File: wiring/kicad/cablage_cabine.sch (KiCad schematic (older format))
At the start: 20 parts, among them J1 Jack90, J2 USB-µ, J3 AlimPlug, SW1 Poussoir, U1 RJ45_Through, U10 Nappe, U11 sortie230, U12 sortie230, U13 FLASH, U14 1200D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

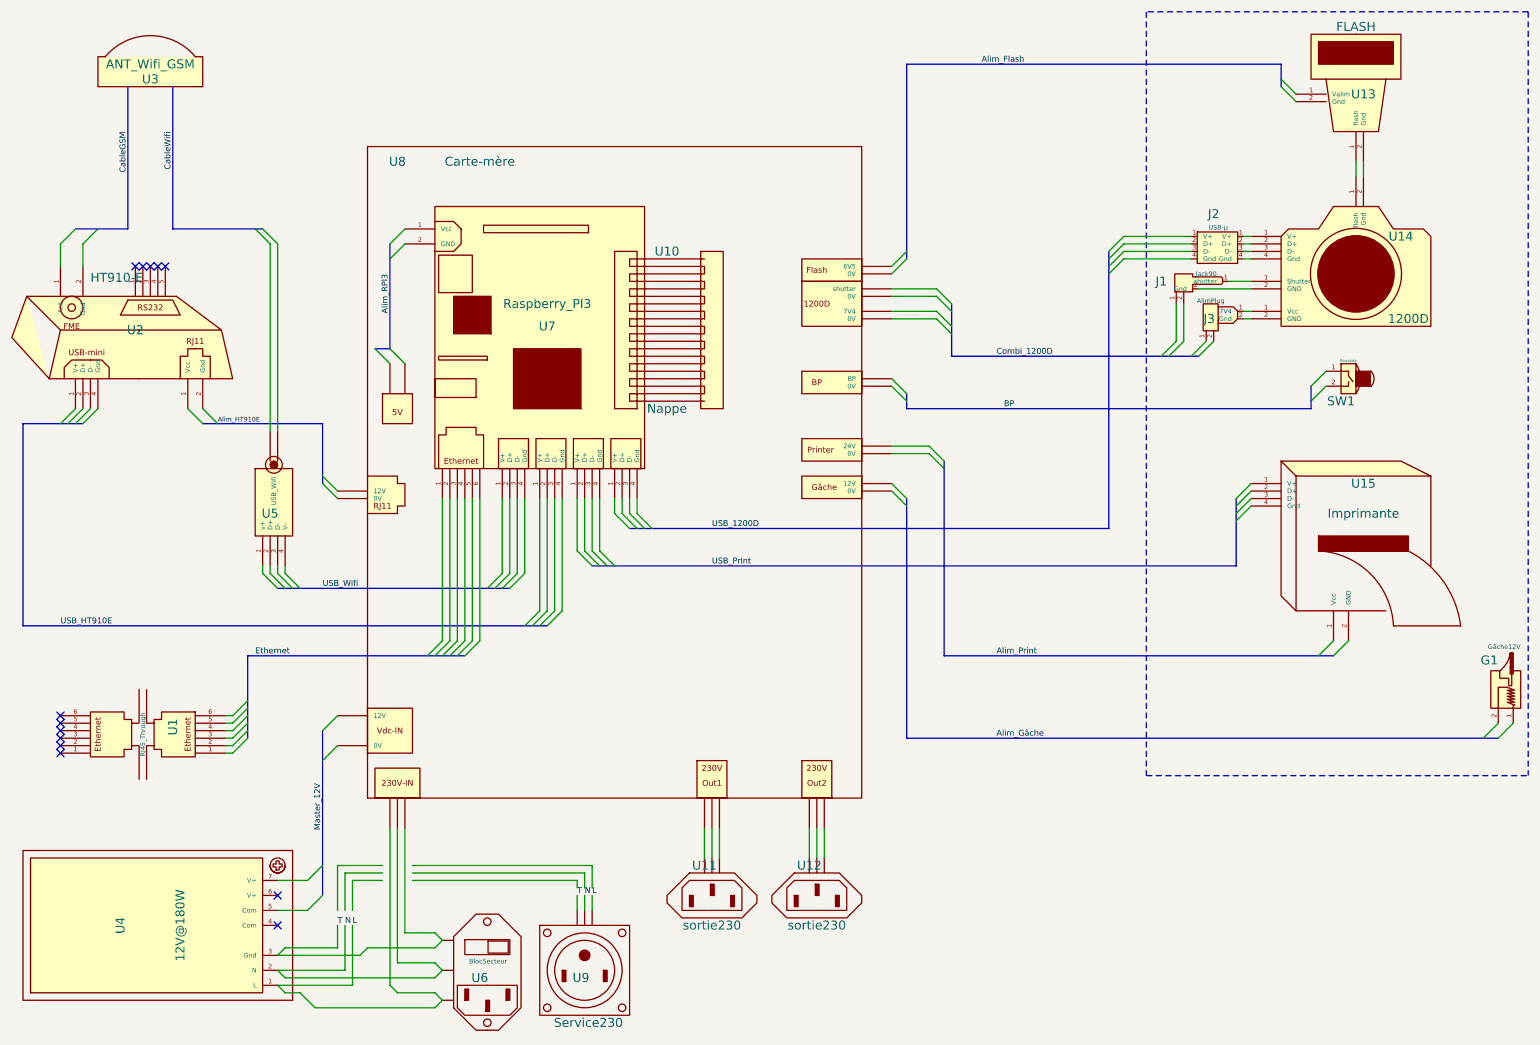
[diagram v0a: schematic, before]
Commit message: * Modification du plan de câblage. Définition des bretelles pour la partie secteur.
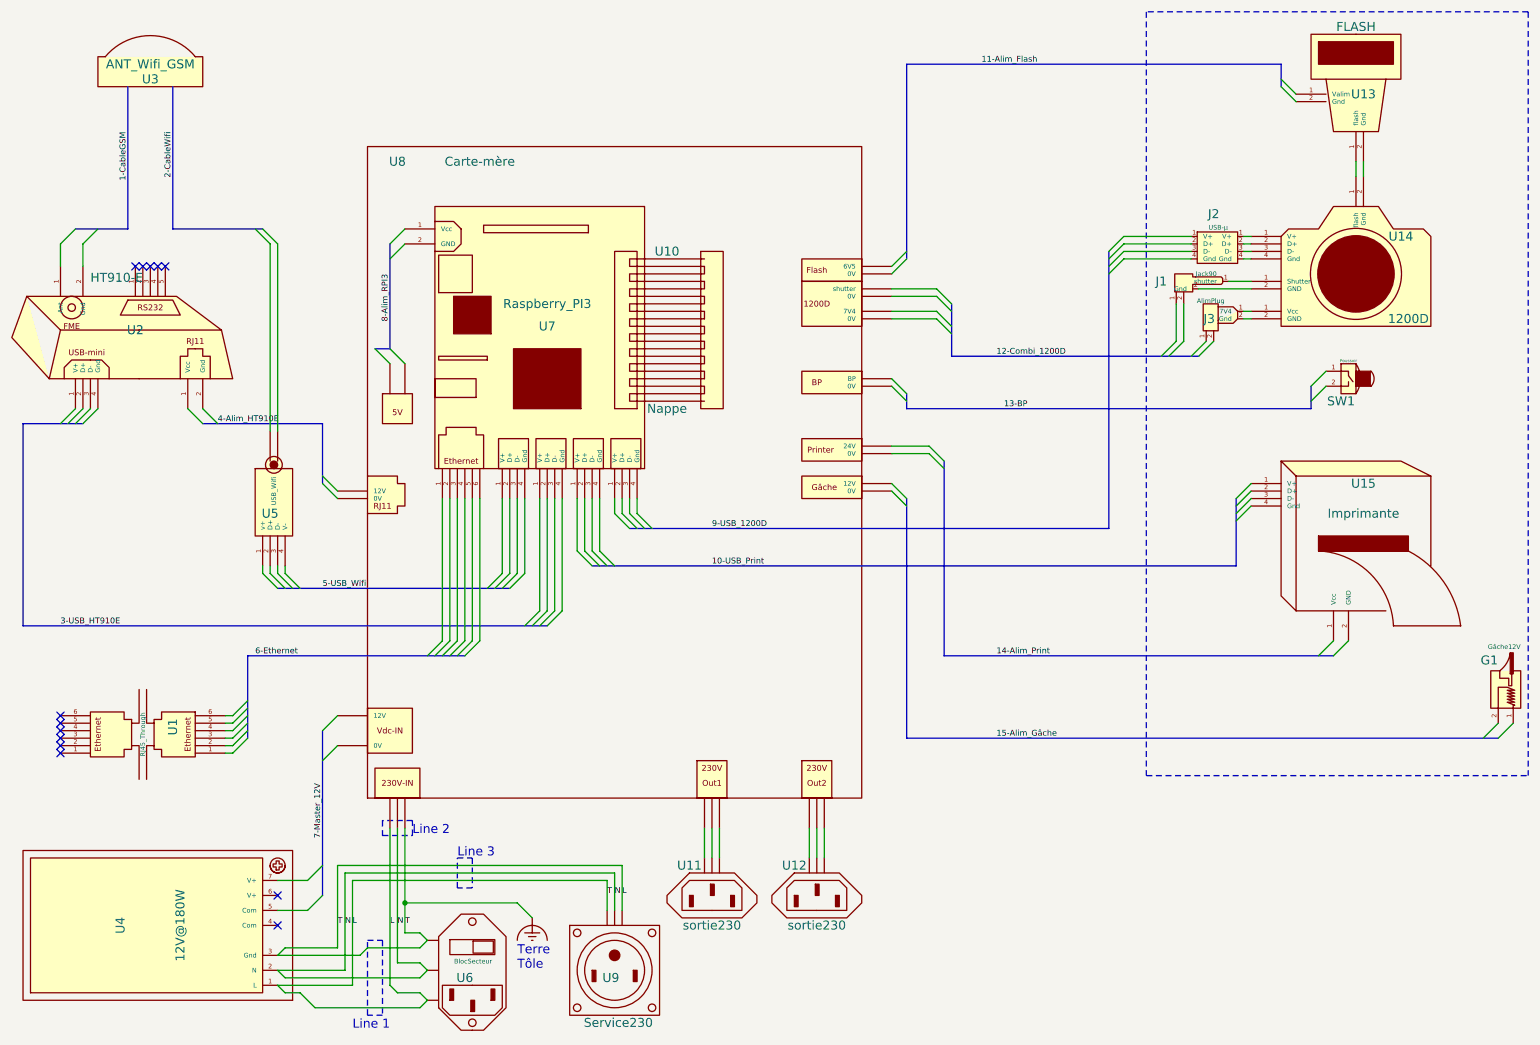
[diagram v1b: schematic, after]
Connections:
- net labels added: 1-CableGSM, 10-USB_Print, 11-Alim_Flash, 12-Combi_1200D, 13-BP, 14-Alim_Print, 15-Alim_Gâche, 2-CableWifi, 3-USB_HT910E, 4-Alim_HT910E, 5-USB_Wifi, 6-Ethernet, 7-Master_12V, 8-Alim_RPI3, 9-USB_1200D, Earth_Clean
- net labels removed: Alim_Flash, Alim_Gâche, Alim_HT910E, Alim_Print, Alim_RPI3, BP, CableGSM, CableWifi, Combi_1200D, Ethernet, Master_12V, USB_1200D, USB_HT910E, USB_Print, USB_Wifi
- wire segments 110 -> 103
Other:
- note added: "Line 1"
- note added: "Line 2"
- note added: "Line 3"
- note added: "Terre\nTôle"
- moved on the sheet: U6, U9
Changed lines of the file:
@@
 U 1 1 58E76E27
 P 5300 6650
-F 0 "U11" H 5250 6800 60  0000 C CNN
+F 0 "U11" H 5150 6800 60  0000 C CNN
 F 1 "sortie230" H 5300 6400 60  0000 C CNN
 F 2 "" H 5315 6650 60  0001 C CNN
@@
 U 1 1 58E76F6F
 P 6000 6650
-F 0 "U12" H 5950 6800 60  0000 C CNN
+F 0 "U12" H 5850 6800 60  0000 C CNN
 F 1 "sortie230" H 6000 6400 60  0000 C CNN
 F 2 "" H 6015 6650 60  0001 C CNN
@@
 L BlocSecteur U6
 U 1 1 58E771CC
-P 3800 7350
-F 0 "U6" H 3750 7450 60  0000 C CNN
-F 1 "BlocSecteur" H 3805 7560 31  0000 C CNN
-F 2 "" H 3815 7250 60  0001 C CNN
-F 3 "" H 3815 7250 60  0001 C CNN
-	1    3800 7350
+P 3700 7350
+F 0 "U6" H 3650 7450 60  0000 C CNN
+F 1 "BlocSecteur" H 3705 7560 31  0000 C CNN
+F 2 "" H 3715 7250 60  0001 C CNN
+F 3 "" H 3715 7250 60  0001 C CNN
+	1    3700 7350
 	1    0    0    -1
 $EndComp
@@
 L Service230 U9
 U 1 1 58E79C50
-P 4450 7150
-F 0 "U9" H 4425 7050 60  0000 C CNN
-F 1 "Service230" H 4475 6750 60  0000 C CNN
-F 2 "" H 5365 7300 60  0001 C CNN
-F 3 "" H 5365 7300 60  0001 C CNN
-	1    4450 7150
+P 4650 7150
+F 0 "U9" H 4625 7050 60  0000 C CNN
+F 1 "Service230" H 4675 6750 60  0000 C CNN
+F 2 "" H 5565 7300 60  0001 C CNN
+F 3 "" H 5565 7300 60  0001 C CNN
+	1    4650 7150
 	1    0    0    -1
 $EndComp
@@
 $EndComp
 Text Label 1700 1600 3    39   ~ 0
-CableWifi
+2-CableWifi
 Text Label 1400 1600 3    39   ~ 0
-CableGSM
+1-CableGSM
 Text Label 950  4900 0    39   ~ 0
-USB_HT910E
-Text Label 2000 3550 0    31   ~ 0
-Alim_HT910E
+3-USB_HT910E
+Text Label 2000 3550 0    39   ~ 0
+4-Alim_HT910E
 Text Label 2250 5100 0    39   ~ 0
-Ethernet
+6-Ethernet
 Text Label 2700 5950 3    39   ~ 0
-Master_12V
+7-Master_12V
 Text Label 2700 4650 0    39   ~ 0
-USB_Wifi
+5-USB_Wifi
 Text Label 3150 2550 3    39   ~ 0
-Alim_RPI3
+8-Alim_RPI3
 Text Label 7100 1150 0    39   ~ 0
-Alim_Flash
+11-Alim_Flash
 Text Label 7200 3100 0    39   ~ 0
-Combi_1200D
+12-Combi_1200D
 Text Label 7250 3450 0    39   ~ 0
-BP
+13-BP
 Text Label 5300 4250 0    39   ~ 0
-USB_1200D
+9-USB_1200D
 Text Label 5300 4500 0    39   ~ 0
-USB_Print
+10-USB_Print
 Text Label 7200 5100 0    39   ~ 0
-Alim_Print
+14-Alim_Print
 Text Label 7200 5650 0    39   ~ 0
-Alim_Gâche
-Wire Wire Line
-	2650 7450 3450 7450
-Wire Wire Line
-	3450 7450 3500 7400
-Wire Wire Line
-	3500 7400 3450 7350
-Wire Wire Line
-	3450 7350 3200 7350
+15-Alim_Gâche
+Wire Wire Line
+	2650 7450 3350 7450
+Wire Wire Line
+	3350 7450 3400 7400
+Wire Wire Line
+	3400 7400 3350 7350
+Wire Wire Line
+	3350 7350 3200 7350
 Wire Wire Line
 	3200 7350 3150 7300
@@
 	3150 7300 3150 6250
 Wire Wire Line
-	3450 7250 3500 7200
-Wire Wire Line
-	3500 7200 3450 7150
-Wire Wire Line
-	3450 7150 3200 7150
+	3350 7250 3400 7200
+Wire Wire Line
+	3400 7200 3350 7150
+Wire Wire Line
+	3350 7150 3200 7150
 Wire Wire Line
 	3200 7150 3200 6250
 Wire Wire Line
-	3450 7050 3500 7000
-Wire Wire Line
-	3500 7000 3450 6950
-Wire Wire Line
-	3450 6950 3250 6950
+	3350 7050 3400 7000
+Wire Wire Line
+	3400 7000 3350 6950
+Wire Wire Line
+	3350 6950 3250 6950
 Wire Wire Line
 	3250 6950 3250 6250
 Wire Wire Line
-	2450 7250 3450 7250
+	2450 7250 3350 7250
 Wire Wire Line
 	2400 7100 2450 7050
@@
 	2450 7350 2550 7350
 Wire Wire Line
-	2400 7300 2900 7300
+	2900 7300 2400 7300
 Wire Wire Line
 	2550 7350 2650 7450
@@
 	2950 7100 3000 7050
 Wire Wire Line
-	3000 7050 3450 7050
+	3000 7050 3350 7050
 Wire Wire Line
 	2450 7050 2800 7050
@@
 	2400 7200 2850 7200
 Wire Wire Line
-	4400 6800 4400 6700
-Wire Wire Line
-	4450 6800 4450 6700
-Wire Wire Line
-	4500 6800 4500 6700
-Text Label 4400 6700 0    39   ~ 0
+	4600 6600 4600 6800
+Wire Wire Line
+	4650 6550 4650 6800
+Wire Wire Line
+	4700 6500 4700 6800
+Text Label 4600 6700 0    39   ~ 0
 T
-Text Label 4450 6700 0    39   ~ 0
+Text Label 4650 6700 0    39   ~ 0
 N
-Text Label 4500 6700 0    39   ~ 0
+Text Label 4700 6700 0    39   ~ 0
 L
 Wire Wire Line
@@
 	5350 6250 5350 6450
 Wire Wire Line
-	4400 6650 4400 6600
-Wire Wire Line
-	4400 6600 3300 6600
-Wire Wire Line
-	4450 6650 4450 6550
-Wire Wire Line
-	4450 6550 3300 6550
-Wire Wire Line
-	4500 6650 4500 6500
-Wire Wire Line
-	4500 6500 3300 6500
-Wire Wire Line
-	3100 6500 2800 6500
-Wire Wire Line
-	2800 6500 2800 6800
-Wire Wire Line
-	2850 6800 2850 6550
-Wire Wire Line
-	2850 6550 3100 6550
-Wire Wire Line
-	2900 6800 2900 6600
-Wire Wire Line
-	2900 6600 3100 6600
-Wire Wire Line
-	2800 7050 2800 6900
-Wire Wire Line
-	2850 7200 2850 6900
-Wire Wire Line
-	2900 7300 2900 6900
+	2900 6600 4600 6600
+Wire Wire Line
+	2850 6550 4650 6550
+Wire Wire Line
+	2800 6500 4700 6500
+Wire Wire Line
+	2800 7050 2800 6500
+Wire Wire Line
+	2850 7200 2850 6550
+Wire Wire Line
+	2900 6600 2900 7300
 NoConn ~ 950  5500
 NoConn ~ 950  5550
@@
 NoConn ~ 950  5700
 NoConn ~ 950  5750
+$Comp
+L Earth_Clean #PWR?
+U 1 1 58ECDAF9
+P 4100 6850
+F 0 "#PWR?" H 4350 6850 50  0001 C CNN
+F 1 "Earth_Clean" H 4400 6700 50  0001 C CNN
+F 2 "" H 4100 6800 50  0001 C CNN
+F 3 "" H 4100 6800 50  0001 C CNN
+	1    4100 6850
+	1    0    0    -1
+$EndComp
+Text Label 3150 6900 0    39   ~ 0
+L
+Text Label 3200 6900 0    39   ~ 0
+N
+Text Label 3250 6900 0    39   ~ 0
+T
+Wire Notes Line
+	3600 6450 3700 6450
+Wire Notes Line
+	3700 6450 3700 6650
+Wire Notes Line
+	3700 6650 3600 6650
+Wire Notes Line
+	3600 6650 3600 6450
+Wire Notes Line
+	3000 7000 3100 7000
+Wire Notes Line
+	3100 7000 3100 7500
+Wire Notes Line
+	3100 7500 3000 7500
+Wire Notes Line
+	3000 7500 3000 7000
+Wire Notes Line
+	3300 6200 3100 6200
+Wire Notes Line
+	3100 6200 3100 6300
+Wire Notes Line
+	3100 6300 3300 6300
+Wire Notes Line
+	3300 6300 3300 6200
+Text Notes 2900 7600 0    60   ~ 0
+Line 1
+Text Notes 3300 6300 0    60   ~ 0
+Line 2
+Text Notes 3600 6450 0    60   ~ 0
+Line 3
+Wire Wire Line
+	4100 6850 4000 6750
+Wire Wire Line
+	4000 6750 3250 6750
+Connection ~ 3250 6750
+Text Notes 4000 7200 0    60   ~ 0
+Terre\nTôle
 $EndSCHEMATC

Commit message: carte mère V2 et câblage V3
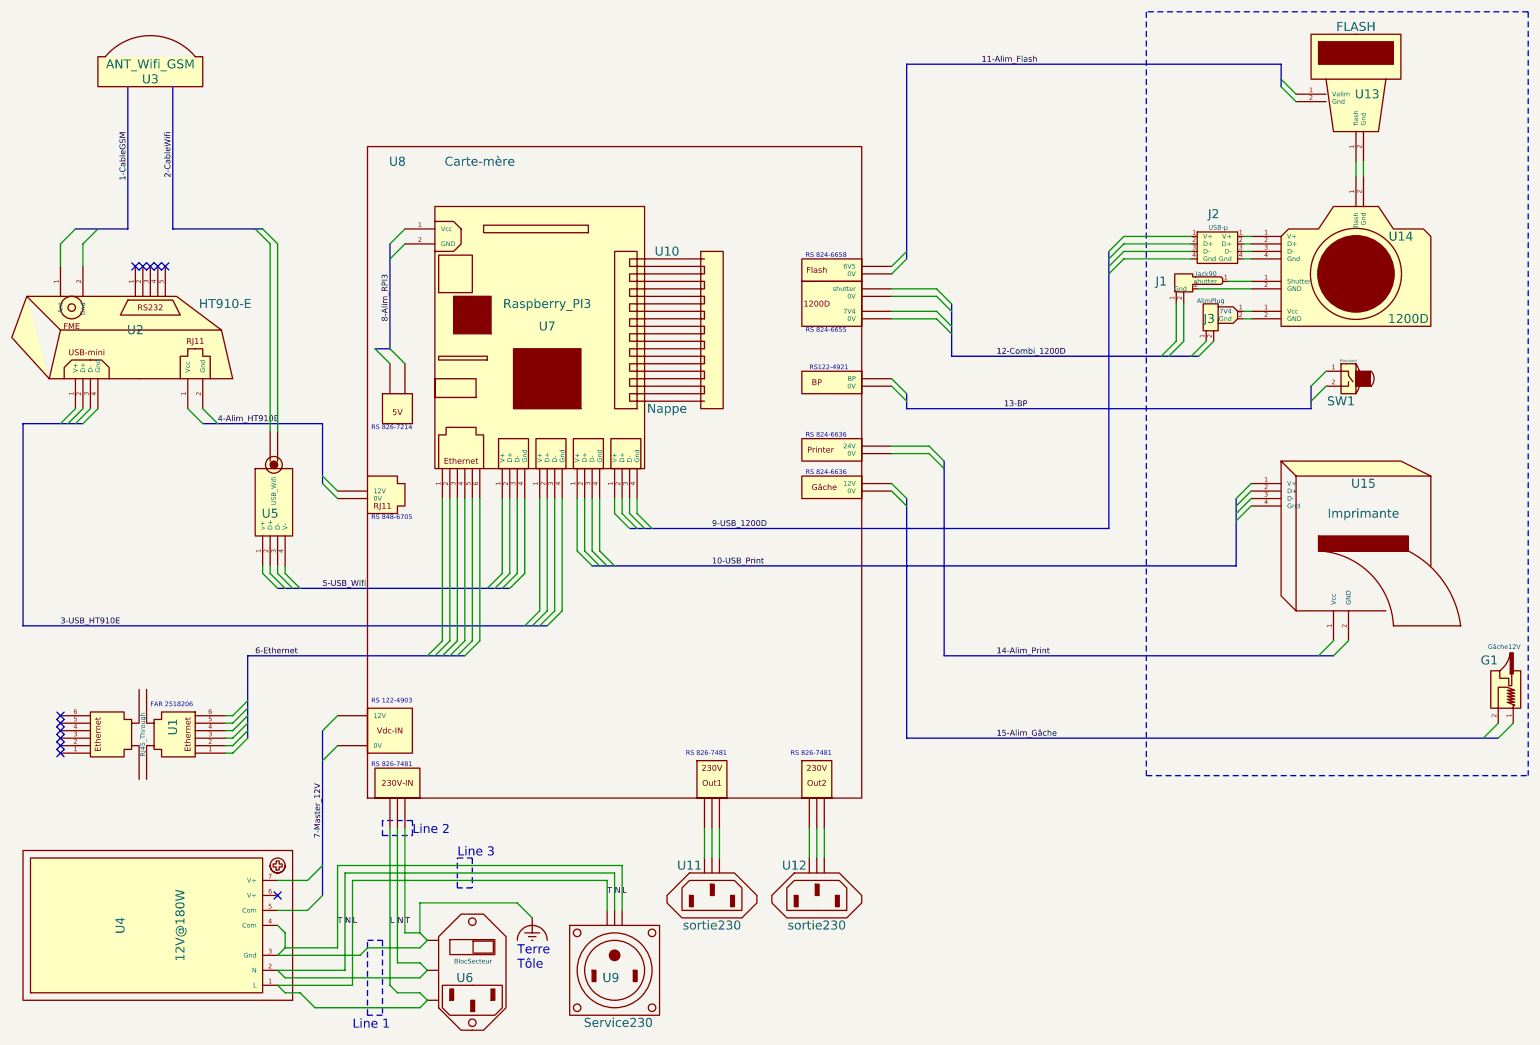
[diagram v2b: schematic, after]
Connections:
- net Earth_Clean: now also U4.4 (Com)
- net at U14.1 (Vcc): now also J3.1; no longer U13.1 (Valim)
- net at J1.1: no longer U14.1 (Vcc)
- net at J2.1 (V+): no longer U14.1 (Vcc)
- net at J3.1: no longer U14.1 (Vcc)
- net at U14.2 (Gnd): now also J3.2; no longer U13.2 (Gnd)
- net at J1.2: no longer U14.2 (Gnd)
- net at J2.2 (D+): no longer U14.2 (Gnd)
- net at J3.2: no longer U14.2 (Gnd)
- new net: U13.1 (Valim), U14.1 (Vcc)
- new net: J1.1, U14.1 (Vcc)
- new net: J2.1 (V+), U14.1 (Vcc)
- new net: U13.2 (Gnd), U14.2 (Gnd)
- new net: J1.2, U14.2 (Gnd)
- new net: J2.2 (D+), U14.2 (Gnd)
- new net: U11.~, U8.~ (x2)
- new net: U12.~, U8.~ (x2)
- no-connect marks 13 -> 12
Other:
- note added: "FAR 2518206"
- note added: "RS 122-4903"
- note added: "RS 824-6636"
- note added: "RS 824-6655"
- note added: "RS 824-6658"
- note added: "RS 826-7214"
- note added: "RS 826-7481"
- note added: "RS 848-6705"
- note added: "RS122-4921"
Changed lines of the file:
@@
 U 1 1 58E663DC
 P 9600 1300
-F 0 "U13" H 9650 1250 60  0000 C CNN
+F 0 "U13" H 9675 1250 60  0000 C CNN
 F 1 "FLASH" H 9600 1700 60  0000 C CNN
 F 2 "" H 9600 1300 60  0001 C CNN
@@
 P 1450 2950
 F 0 "U2" H 1450 2975 60  0000 C CNN
-F 1 "HT910-E" H 1325 3325 60  0000 C CNN
+F 1 "HT910-E" H 2050 3150 60  0000 C CNN
 F 2 "" H 1450 3050 60  0001 C CNN
 F 3 "" H 1450 3050 60  0001 C CNN
@@
 $EndComp
 NoConn ~ 2400 6700
-NoConn ~ 2400 6900
 Entry Wire Line
 	3250 2250 3150 2350
@@
 Wire Wire Line
 	4100 6850 4000 6750
-Wire Wire Line
-	4000 6750 3250 6750
-Connection ~ 3250 6750
 Text Notes 4000 7200 0    60   ~ 0
 Terre\nTôle
+Wire Wire Line
+	4000 6750 3350 6750
+Wire Wire Line
+	3350 6750 3350 6950
+Wire Wire Line
+	2400 6900 2450 6950
+Wire Wire Line
+	2450 6950 2450 7050
+Text Notes 3025 3600 0    31   ~ 0
+RS 826-7214
+Text Notes 3025 4200 0    31   ~ 0
+RS 848-6705
+Text Notes 3025 5425 0    31   ~ 0
+RS 122-4903
+Text Notes 3025 5850 0    31   ~ 0
+RS 826-7481
+Text Notes 5125 5775 0    31   ~ 0
+RS 826-7481
+Text Notes 5825 5775 0    31   ~ 0
+RS 826-7481
+Text Notes 5925 3900 0    31   ~ 0
+RS 824-6636
+Text Notes 5925 3650 0    31   ~ 0
+RS 824-6636
+Text Notes 5950 3200 0    31   ~ 0
+RS122-4921
+Text Notes 5925 2950 0    31   ~ 0
+RS 824-6655
+Text Notes 5925 2450 0    31   ~ 0
+RS 824-6658
+Text Notes 1550 5450 0    31   ~ 0
+FAR 2518206
 $EndSCHEMATC
